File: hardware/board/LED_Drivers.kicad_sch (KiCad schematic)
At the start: 69 parts

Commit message: Final touches before being ready for ordering
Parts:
- R? (x2): value 1.8k -> 1k8
- R? (x4): value 1.2k -> 1k2
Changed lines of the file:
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@@
       (effects (font (size 1.27 1.27)) (justify left))
     )
-    (property "Value" "1.8k" (at 87.63 186.055 0)
+    (property "Value" "1k8" (at 87.63 186.055 0)
       (effects (font (size 1.27 1.27)) (justify left))
     )
@@
       (effects (font (size 1.27 1.27)) (justify left))
     )
-    (property "Value" "1.2k" (at 120.65 186.055 0)
+    (property "Value" "1k2" (at 120.65 186.055 0)
       (effects (font (size 1.27 1.27)) (justify left))
     )
@@
       (effects (font (size 1.27 1.27)) (justify left))
     )
-    (property "Value" "1.2k" (at 224.79 71.755 0)
+    (property "Value" "1k2" (at 224.79 71.755 0)
       (effects (font (size 1.27 1.27)) (justify left))
     )
@@
       (effects (font (size 1.27 1.27)) (justify left))
     )
-    (property "Value" "1.8k" (at 87.63 130.175 0)
+    (property "Value" "1k8" (at 87.63 130.175 0)
       (effects (font (size 1.27 1.27)) (justify left))
     )
@@
       (effects (font (size 1.27 1.27)) (justify left))
     )
-    (property "Value" "1.2k" (at 120.65 130.175 0)
+    (property "Value" "1k2" (at 120.65 130.175 0)
       (effects (font (size 1.27 1.27)) (justify left))
     )
@@
       (effects (font (size 1.27 1.27)) (justify left))
     )
-    (property "Value" "1.2k" (at 104.14 71.755 0)
-      (effects (font (size 1.27 1.27)) (justify left))
-    )
+    (property "Value" "1k2" (at 104.14 71.755 0)
+      (effects (font (size 1.27 1.27)) (justify left))
+    )

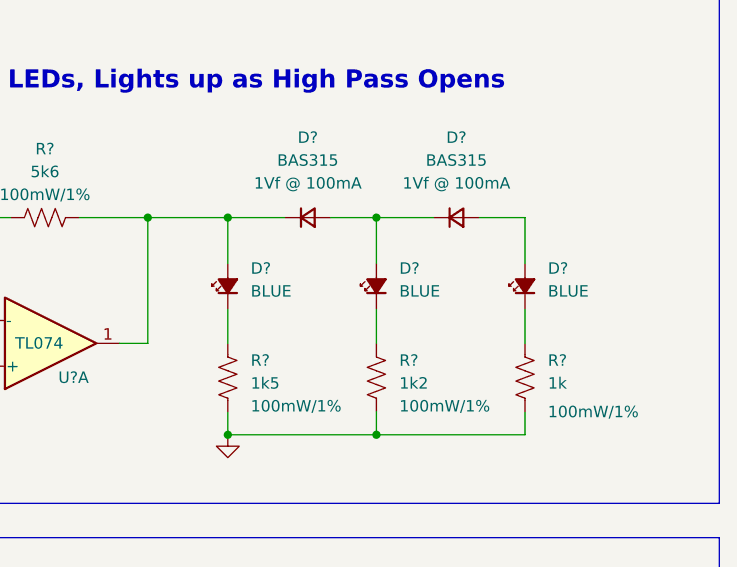
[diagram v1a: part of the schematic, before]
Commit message: hardware: minor fixes and aesthetic updates
- Fix HP LEDs being backwards
- Switch power header, pot, and jack footprints to longpad variants
- Make the text size on the front side larger
- Add "red" and "blue" text next to respective LEDs on front side
- Adjusted zone thermal spoke for better connection to GND pads
- Squished the solder jumpers for instability type closer together
- Minor adjustments to traces to accommodate longpad footprints
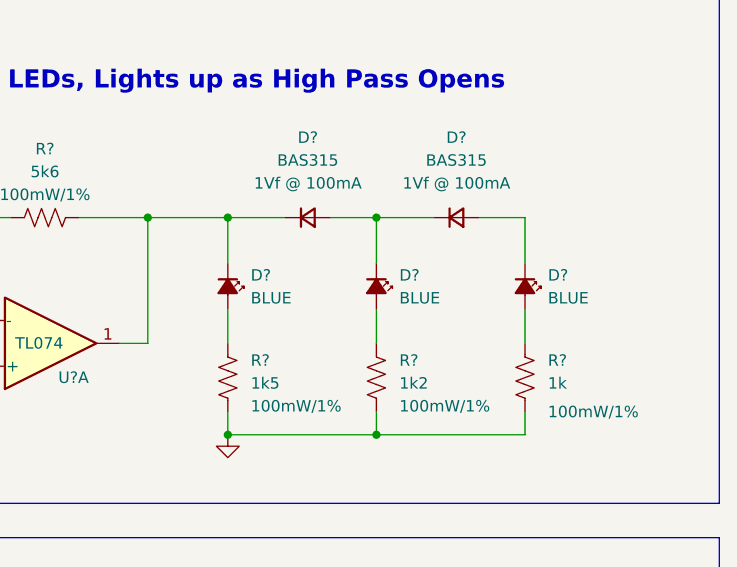
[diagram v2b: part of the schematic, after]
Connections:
- net at D?.1 (K), R?.1, U?.1: now also D?.1 (K); no longer D?.2 (A)
- net at R?.1: now also D?.2 (A); no longer D?.1 (K) (x3)
- net at D?.1 (K), D?.2 (A): now also D?.1 (K); no longer D?.2 (A)
- net at D?.2 (A): now also D?.1 (K); no longer D?.2 (A)
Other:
- moved on the sheet: D?
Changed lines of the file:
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@@
     )
   )
-  (symbol (lib_id "Device:LED_Small_Filled") (at 222.25 60.96 90) (unit 1)
-    (in_bom yes) (on_board yes) (dnp no)
-    (property "Reference" "D?" (at 224.79 58.9915 90)
-      (effects (font (size 1.27 1.27)) (justify right))
-    )
-    (property "Value" "BLUE" (at 224.79 61.5315 90)
-      (effects (font (size 1.27 1.27)) (justify right))
+  (symbol (lib_id "Device:LED_Small_Filled") (at 222.25 60.96 270) (unit 1)
+    (in_bom yes) (on_board yes) (dnp no) (fields_autoplaced)
+    (property "Reference" "D?" (at 224.79 59.7535 90)
+      (effects (font (size 1.27 1.27)) (justify left))
+    )
+    (property "Value" "BLUE" (at 224.79 62.2935 90)
+      (effects (font (size 1.27 1.27)) (justify left))
     )
     (property "Footprint" "winterbloom:LED_0805_Kingbright_APT2012" (at 222.25 60.96 90)
@@
       (effects (font (size 1.27 1.27)) hide)
     )
-    (property "Rating" "blue" (at 224.79 64.0715 90)
+    (property "Rating" "blue" (at 219.71 57.8485 90)
       (effects (font (size 1.27 1.27)) (justify right) hide)
     )
@@
     )
   )
-  (symbol (lib_id "Device:LED_Small_Filled") (at 205.74 60.96 90) (unit 1)
-    (in_bom yes) (on_board yes) (dnp no)
-    (property "Reference" "D?" (at 208.28 58.9915 90)
-      (effects (font (size 1.27 1.27)) (justify right))
-    )
-    (property "Value" "BLUE" (at 208.28 61.5315 90)
-      (effects (font (size 1.27 1.27)) (justify right))
+  (symbol (lib_id "Device:LED_Small_Filled") (at 205.74 60.96 270) (unit 1)
+    (in_bom yes) (on_board yes) (dnp no) (fields_autoplaced)
+    (property "Reference" "D?" (at 208.28 59.7535 90)
+      (effects (font (size 1.27 1.27)) (justify left))
+    )
+    (property "Value" "BLUE" (at 208.28 62.2935 90)
+      (effects (font (size 1.27 1.27)) (justify left))
     )
     (property "Footprint" "winterbloom:LED_0805_Kingbright_APT2012" (at 205.74 60.96 90)
@@
       (effects (font (size 1.27 1.27)) hide)
     )
-    (property "Rating" "blue" (at 208.28 64.0715 90)
+    (property "Rating" "blue" (at 203.2 57.8485 90)
       (effects (font (size 1.27 1.27)) (justify right) hide)
     )
@@
     )
   )
-  (symbol (lib_id "Device:LED_Small_Filled") (at 238.76 60.96 90) (unit 1)
-    (in_bom yes) (on_board yes) (dnp no)
-    (property "Reference" "D?" (at 241.3 58.9915 90)
-      (effects (font (size 1.27 1.27)) (justify right))
-    )
-    (property "Value" "BLUE" (at 241.3 61.5315 90)
-      (effects (font (size 1.27 1.27)) (justify right))
+  (symbol (lib_id "Device:LED_Small_Filled") (at 238.76 60.96 270) (unit 1)
+    (in_bom yes) (on_board yes) (dnp no) (fields_autoplaced)
+    (property "Reference" "D?" (at 241.3 59.7535 90)
+      (effects (font (size 1.27 1.27)) (justify left))
+    )
+    (property "Value" "BLUE" (at 241.3 62.2935 90)
+      (effects (font (size 1.27 1.27)) (justify left))
     )
     (property "Footprint" "winterbloom:LED_0805_Kingbright_APT2012" (at 238.76 60.96 90)
@@
       (effects (font (size 1.27 1.27)) hide)
     )
-    (property "Rating" "blue" (at 241.3 64.0715 90)
+    (property "Rating" "blue" (at 236.22 57.8485 90)
       (effects (font (size 1.27 1.27)) (justify right) hide)
     )

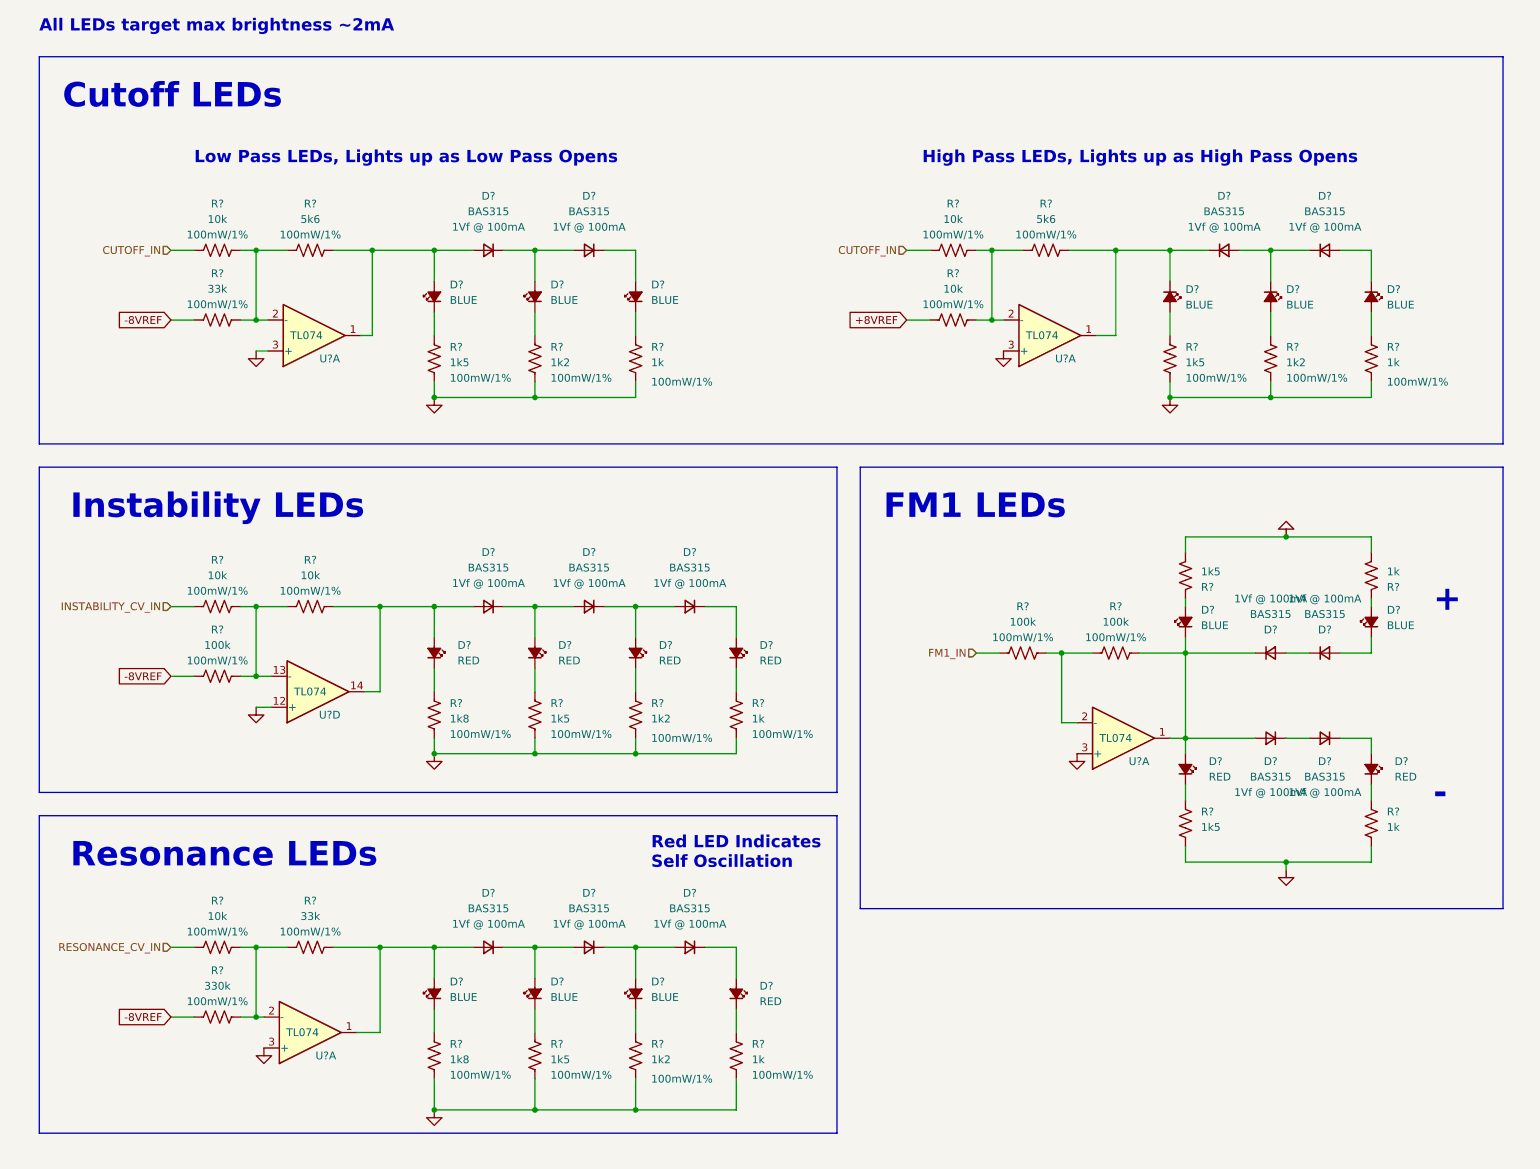
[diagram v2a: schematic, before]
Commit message: Updated Schematic
-Added R935, R936, and Q901 to make resonance self oscillation LED turn on sharply

-Moved D929, D930, and added R933, R934 to make FM1 LED more sensitive

-Changed FM1 Attenuverter and added R410 and R411 to make FM1 Knob have some curve/deadzone

-Changed Resonance VCA output and added R623 and R624 to make resonance VCA output higher voltage to avoid opamp offset being significant .

-Added testing documents
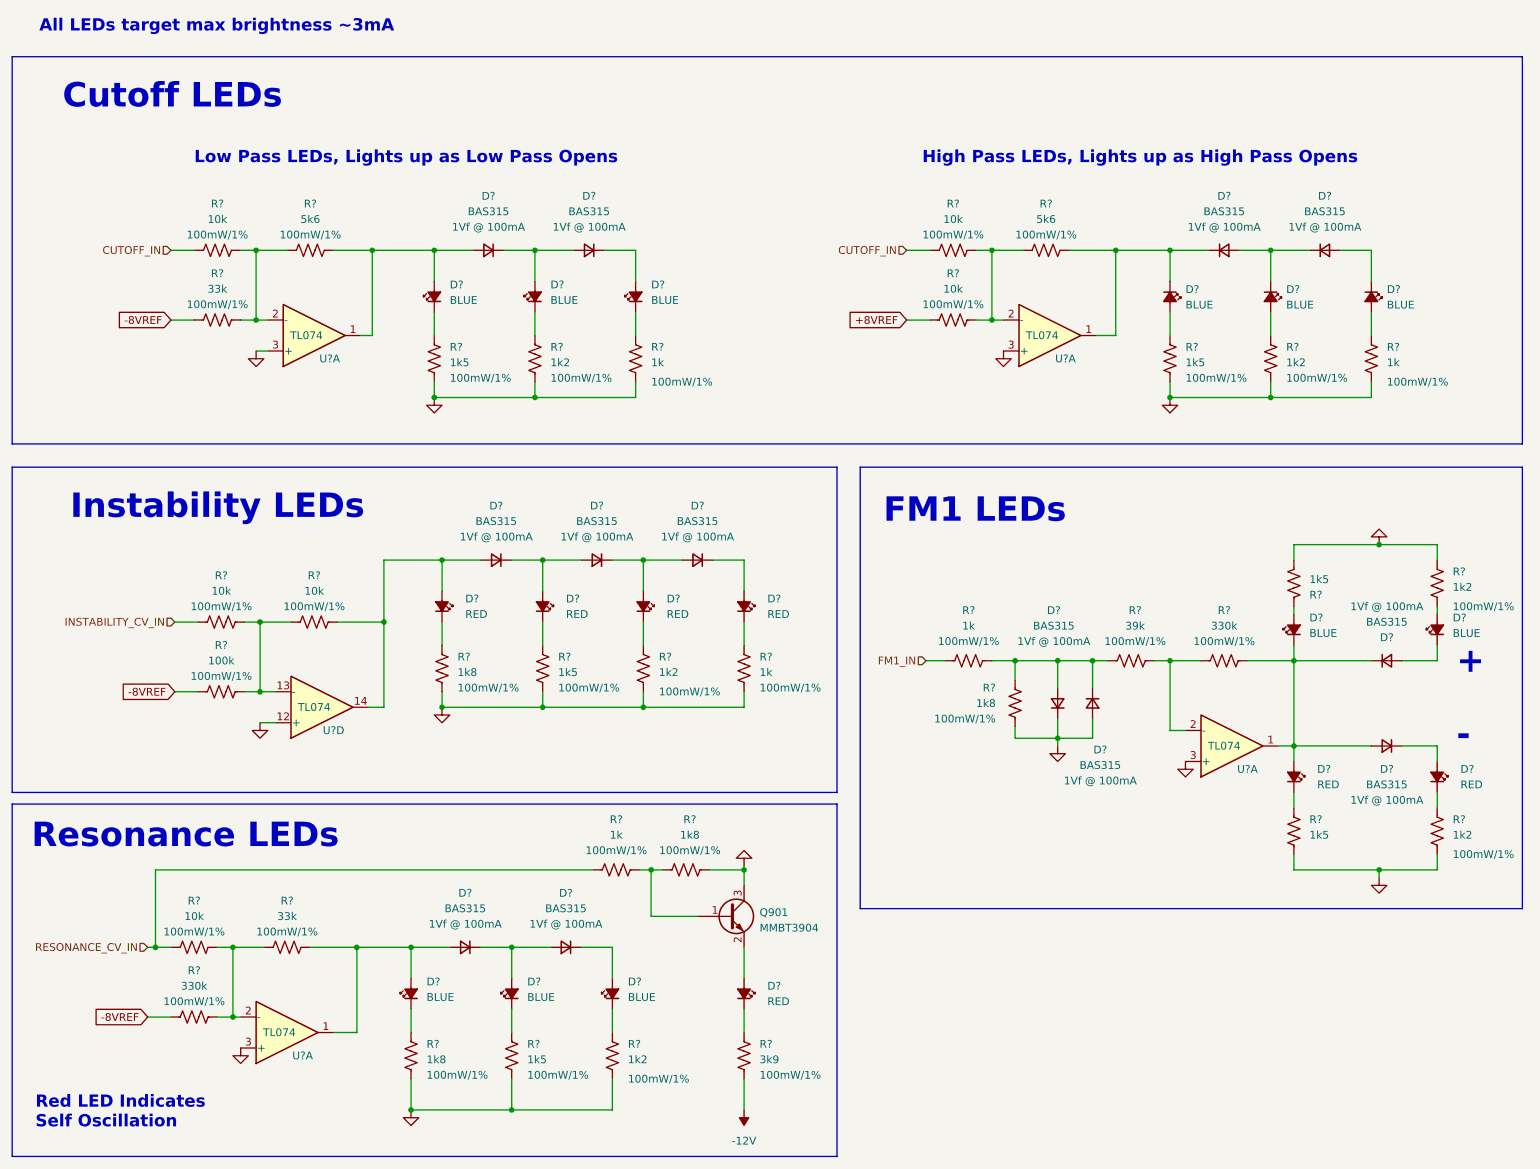
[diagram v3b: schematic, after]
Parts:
- removed D?: BAS315, winterbloom:D_SOD-323, symbol Device:D_Small
- removed R? (x3): 1k, winterbloom:R_0603_HandSolder, symbol Device:R_US
- removed R? (x2): 100k, winterbloom:R_0603_HandSolder, symbol Device:R_US
- added Q901: MMBT3904, Package_TO_SOT_SMD:SOT-23, symbol Transistor_BJT:MMBT3904
- added R? (x2): 1k8, winterbloom:R_0603_HandSolder, symbol Device:R_US
- added R? (x2): 1k, winterbloom:R_0603_HandSolder, symbol Device:R_US
- added R?: 330k, winterbloom:R_0603_HandSolder, symbol Device:R_US
- added R? (x2): 1k2, winterbloom:R_0603_HandSolder, symbol Device:R_US
- added R?: 3k9, winterbloom:R_0603_HandSolder, symbol Device:R_US
- added R?: 39k, winterbloom:R_0603_HandSolder, symbol Device:R_US
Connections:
- net FM1_IN: now also R?.1
- net GND: now also D?.1 (K), D?.2 (A), Q901.3 (C), R?.1, R?.1, R?.2, R?.2
- net RESONANCE_CV_IN: now also R?.1
- net at D?.1 (K): now also D?.2 (A); no longer D?.2 (A) (x2)
- net at D?.1 (K), D?.1 (K), D?.2 (A)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: now also R?.1
- net at D?.1 (K): now also R?.1 (x2)
- net at D?.1 (K): now also D?.2 (A), R?.1, R?.2, R?.2; no longer D?.2 (A)
- net at D?.2 (A): now also R?.2
- net at U?.2 (-): now also R?.2, R?.2
- net at D?.2 (A): now also Q901.2 (E)
- new net: Q901.1 (B), R?.1, R?.2
- new net -12V: R?.2
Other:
- note added: "All LEDs target max brightness ~3mA"
- note removed: "All LEDs target max brightness ~2mA"
- moved on the sheet: D?, R?, U?A, U?D

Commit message: Updated PCB to add and routed new components.
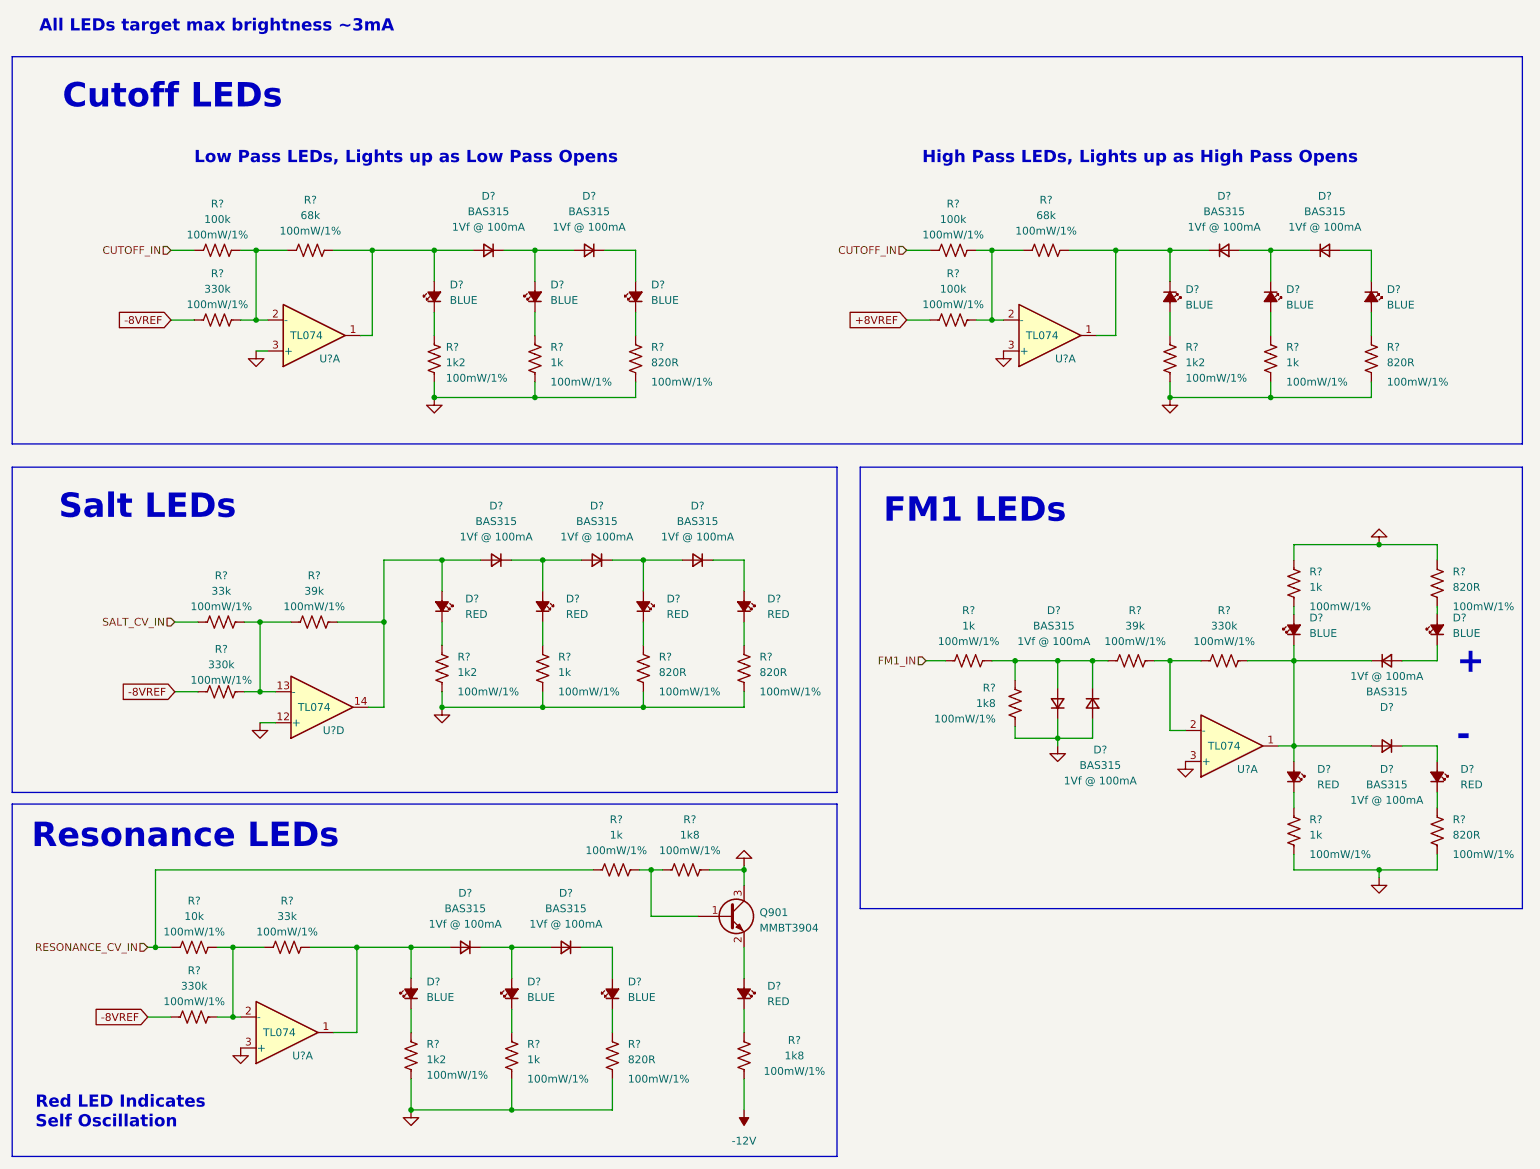
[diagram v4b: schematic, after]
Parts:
- removed R? (x2): 5k6, winterbloom:R_0603_HandSolder, symbol Device:R_US
- removed R? (x6): 1k5, winterbloom:R_0603_HandSolder, symbol Device:R_US
- removed R? (x5): 10k, winterbloom:R_0603_HandSolder, symbol Device:R_US
- removed R?: 33k, winterbloom:R_0603_HandSolder, symbol Device:R_US
- removed R? (x3): 1k, winterbloom:R_0603_HandSolder, symbol Device:R_US
- removed R? (x2): 1k8, winterbloom:R_0603_HandSolder, symbol Device:R_US
- removed R?: 100k, winterbloom:R_0603_HandSolder, symbol Device:R_US
- removed R? (x6): 1k2, winterbloom:R_0603_HandSolder, symbol Device:R_US
- removed R?: 3k9, winterbloom:R_0603_HandSolder, symbol Device:R_US
- added R? (x6): 1k, winterbloom:R_0603_HandSolder, symbol Device:R_US
- added R? (x4): 1k2, winterbloom:R_0603_HandSolder, symbol Device:R_US
- added R? (x2): 330k, winterbloom:R_0603_HandSolder, symbol Device:R_US
- added R? (x7): 820R, winterbloom:R_0603_HandSolder, symbol Device:R_US
- added R?: 33k, winterbloom:R_0603_HandSolder, symbol Device:R_US
- added R? (x3): 100k, winterbloom:R_0603_HandSolder, symbol Device:R_US
- added R? (x2): 68k, winterbloom:R_0603_HandSolder, symbol Device:R_US
- added R?: 39k, winterbloom:R_0603_HandSolder, symbol Device:R_US
- added R?: 1k8, winterbloom:R_0603_HandSolder, symbol Device:R_US
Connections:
- net +8VREF: now also R?.2
- net -12V: now also R?.1
- net -8VREF: now also R?.2, R?.2
- net CUTOFF_IN: now also R?.2, R?.2
- net GND: now also R?.1, R?.1, R?.2, R?.2, R?.2, R?.2, R?.2, R?.2, R?.2, R?.2, R?.2, R?.2, R?.2, R?.2, R?.2, R?.2, R?.2
- net at D?.1 (K): now also R?.1 (x12)
- net at D?.1 (K), D?.1 (K), U?.1: now also R?.2
- net at U?.2 (-): now also R?.1, R?.1, R?.1 (x2)
- net at D?.2 (A): now also R?.1 (x3)
- net at U?.13 (-): now also R?.1, R?.1, R?.1
- net at D?.2 (A), D?.2 (A), U?.14: now also R?.2
- net at D?.2 (A), D?.2 (A), U?.1: now also R?.2
- net at D?.2 (A): now also R?.2 (x2)
- net at D?.1 (K): now also R?.2
- new net SALT_CV_IN: R?.2
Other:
- note added: "Salt LEDs"
- note removed: "Instability LEDs"
